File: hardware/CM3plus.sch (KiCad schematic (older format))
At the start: 40 parts, among them J1 USB_B_Micro, J5 HD44780, J6 OLED, J7 Barrel_Jack, J8 Buttons, U1 DDR2_SODIMM_CM_3_Lite, U2 PAM2306AYPKE, U3 AP7115-25SEG

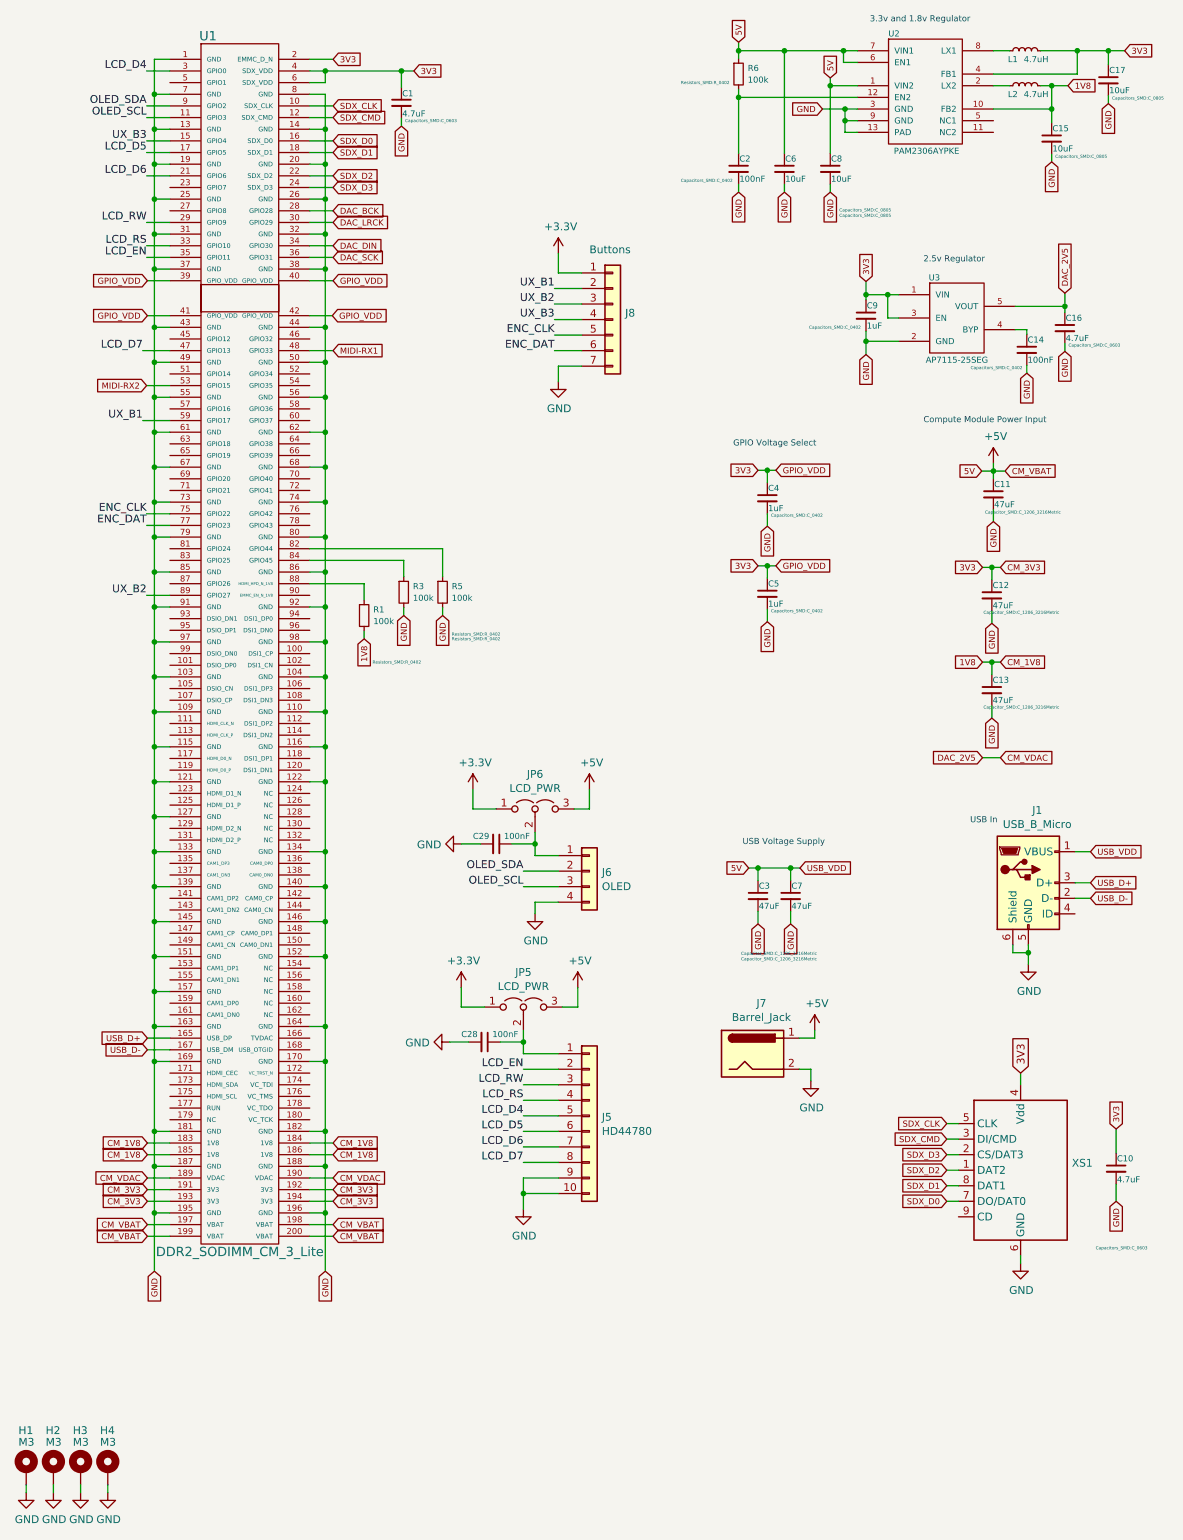
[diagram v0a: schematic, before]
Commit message: Cleaning up the power section
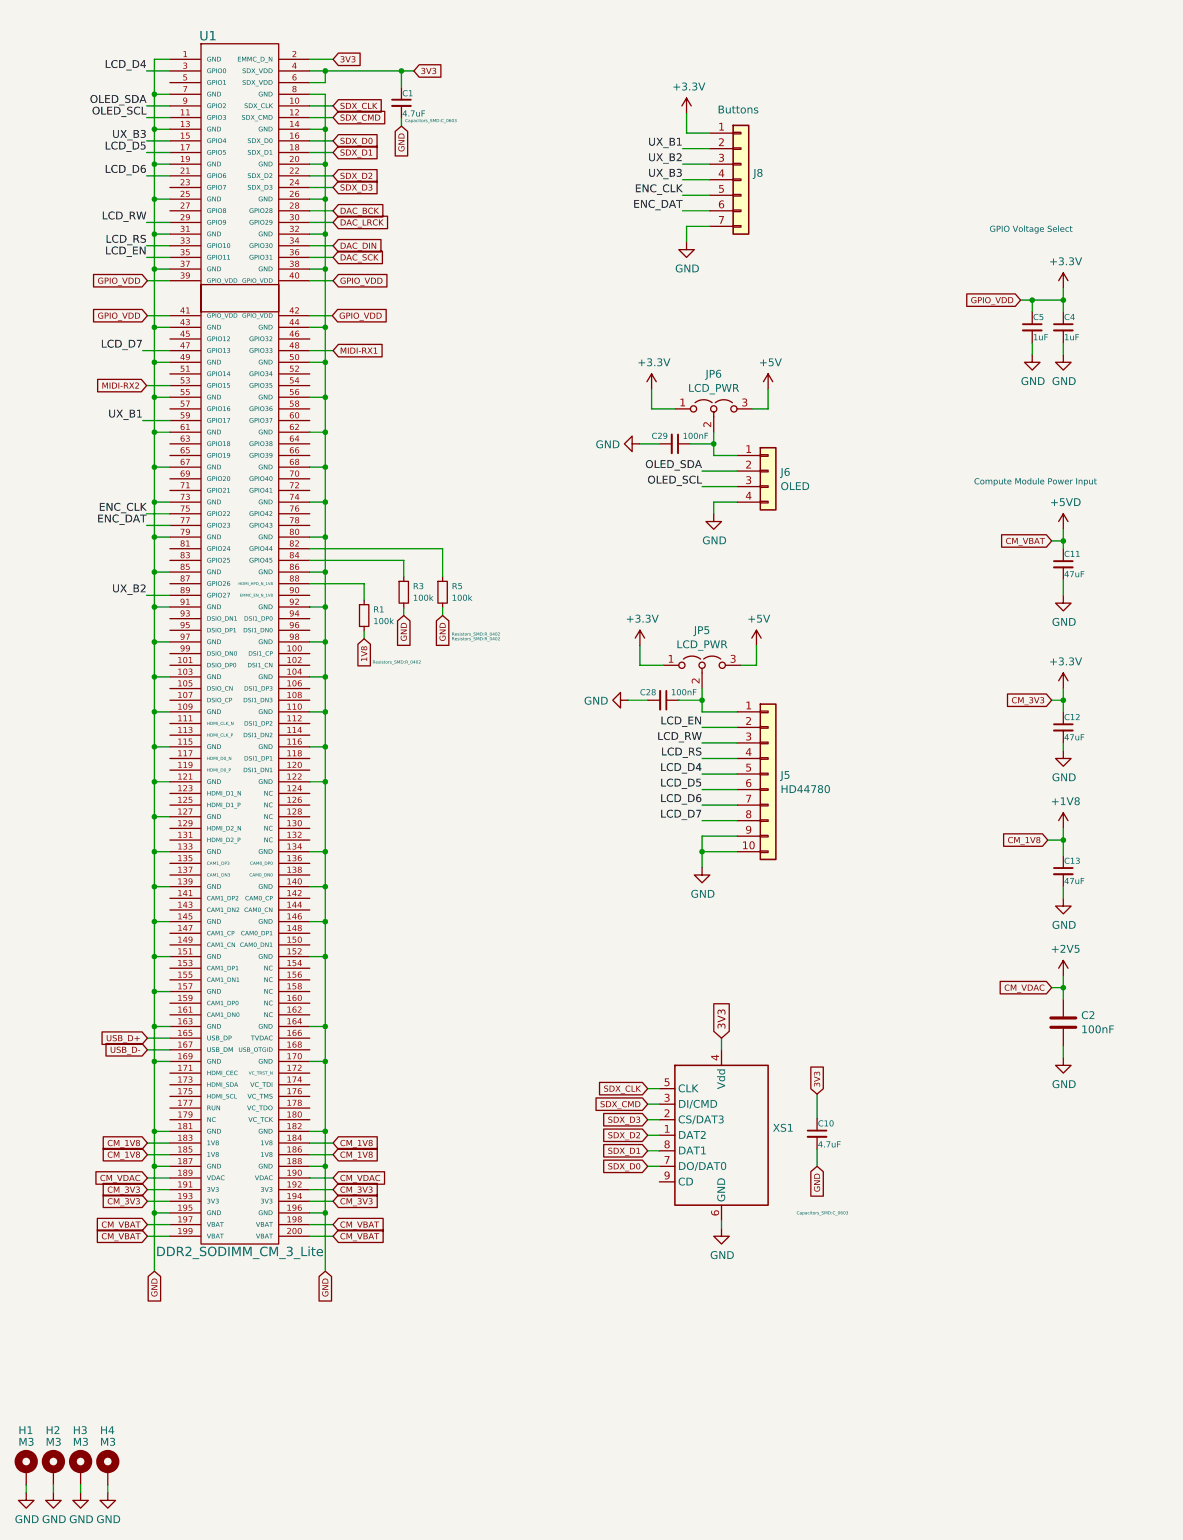
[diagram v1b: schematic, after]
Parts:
- removed C14, C2: 100nF, Capacitors_SMD:C_0402, symbol Device:C_Small
- removed C15, C17, C6, C8: 10uF, Capacitors_SMD:C_0805, symbol Device:C_Small
- removed C16: 4.7uF, Capacitors_SMD:C_0603, symbol Device:C_Small
- removed C3, C7: 47uF, Capacitor_SMD:C_1206_3216Metric, symbol Device:C_Small
- removed C9: 1uF, Capacitors_SMD:C_0402, symbol Device:C_Small
- removed J1: USB_B_Micro, Connector_USB:USB_Micro-B_Amphenol_10103594-0001LF_Horizontal, symbol Connector:USB_B_Micro
- removed J7: Barrel_Jack, Connector_BarrelJack:BarrelJack_Horizontal, symbol Connector:Barrel_Jack
- removed L1, L2: 4.7uH, Pi-Library:SRN4018-4R7M, symbol Device:L_Small
- removed R6: 100k, Resistors_SMD:R_0402, symbol Device:R_Small
- removed U2: PAM2306AYPKE, Pi-Library:PAM2306AYPKE, symbol voltage_reg:PAM2306AYPKE
- removed U3: AP7115-25SEG, Pi-Library:AP7115-25SEG-7, symbol voltage_reg:AP7115-25SEG
- added C2: 100nF, Capacitor_SMD:C_0402_1005Metric, symbol Device:C
- C4, C5: footprint Capacitors_SMD:C_0402 -> Capacitor_SMD:C_0402_1005Metric
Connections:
- net +3V3: now also C12.1, C4.1, C5.1, U1.191 (3V3), U1.192 (3V3), U1.193 (3V3), U1.194 (3V3), U1.39 (GPIO_VDD), U1.40 (GPIO_VDD), U1.41 (GPIO_VDD), U1.42 (GPIO_VDD)
- net +5V: no longer C11.1, U1.197 (VBAT), U1.198 (VBAT), U1.199 (VBAT), U1.200 (VBAT)
- net 1V8: no longer C13.1, U1.183 (1V8), U1.184 (1V8), U1.185 (1V8), U1.186 (1V8)
- net 3V3: no longer C12.1, C4.1, C5.1, U1.191 (3V3), U1.192 (3V3), U1.193 (3V3), U1.194 (3V3), U1.39 (GPIO_VDD), U1.40 (GPIO_VDD), U1.41 (GPIO_VDD), U1.42 (GPIO_VDD)
- net GND: now also C2.2
- net CM_VDAC renamed +2V5
- net +2V5: now also C2.1
- new net +1V8: C13.1, U1.183 (1V8), U1.184 (1V8), U1.185 (1V8), U1.186 (1V8)
- new net +5VD: C11.1, U1.197 (VBAT), U1.198 (VBAT), U1.199 (VBAT), U1.200 (VBAT)
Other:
- note removed: "2.5v Regulator"
- note removed: "3.3v and 1.8v Regulator"
- note removed: "USB In"
- note removed: "USB Voltage Supply"
- moved on the sheet: C10, C11, C12, C13, C28, C29, C4, C5, J5, J6, J8, JP5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
